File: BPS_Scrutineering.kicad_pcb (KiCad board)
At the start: 2 copper layers, 75 x 75 mm, 54 parts, among them SW1 SW_DIP_x07, SW2 SW_DIP_x07

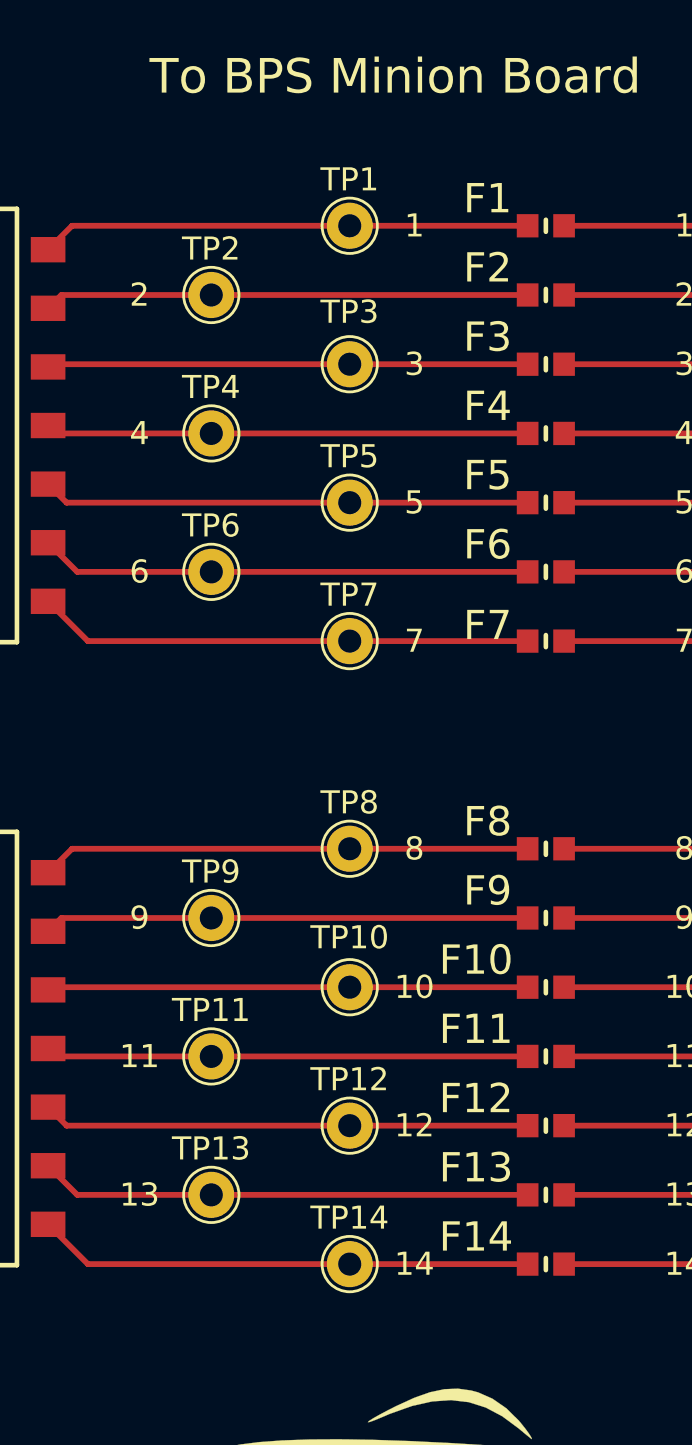
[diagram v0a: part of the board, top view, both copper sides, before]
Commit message: Changed testpoint footprints to match commonly-used testpoints
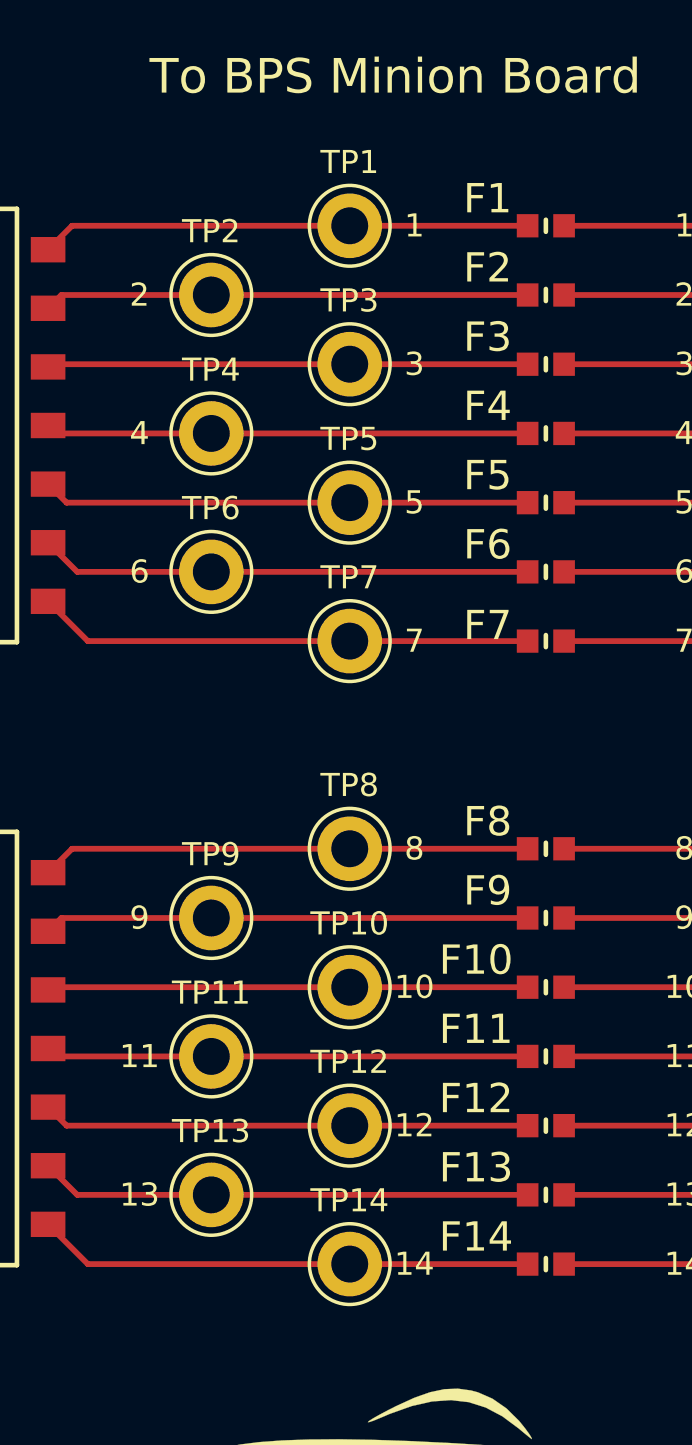
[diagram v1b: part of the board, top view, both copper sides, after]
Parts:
- TP1, TP10, TP11, TP12, TP13, TP14, TP2, TP3, TP4, TP5, TP6, TP7, TP8, TP9: footprint TestPoint:TestPoint_THTPad_D2.0mm_Drill1.0mm -> TestPoint:TestPoint_Keystone_5005-5009_Compact

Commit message: Finished Schematic
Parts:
- removed Dr_Hallock1: Dr. Hallock, UTSVT_Special:Hallock_Image
- removed H1, H2, H3, H4: MountingHole, MountingHole:MountingHole_3mm_Pad
- removed JC1, JC2, JC3, JC4: Conn_01x07, UTSVT_Connectors:Molex_Microfit+_01x07_Horizontal
- removed UTSVT_Logo1: UTSVT, UTSVT_Special:UTSVT_Logo_Symbol
- added F29: PTC Fuse, footprints:FUSC1810X100N, F.Cu at (171.2, 137.8)
- added F30: PTC Fuse, footprints:FUSC1810X100N, F.Cu at (171.2, 140.4)
- added F31: PTC Fuse, footprints:FUSC1810X100N, F.Cu at (171.2, 143.1)
- added F32: PTC Fuse, footprints:FUSC1810X100N, F.Cu at (171.2, 145.7)
- added F33: PTC Fuse, footprints:FUSC1810X100N, F.Cu at (171.2, 148.4)
- added F34: PTC Fuse, footprints:FUSC1810X100N, F.Cu at (171.2, 151.1)
- added F35: PTC Fuse, footprints:FUSC1810X100N, F.Cu at (171.2, 153.7)
- added F36: PTC Fuse, footprints:FUSC1810X100N, F.Cu at (171.2, 156.4)
- added F37: PTC Fuse, footprints:FUSC1810X100N, F.Cu at (100.6, 18.8)
- added F38: PTC Fuse, footprints:FUSC1810X100N, F.Cu at (100.6, 21.8)
- added F39: PTC Fuse, footprints:FUSC1810X100N, F.Cu at (100.6, 24.8)
- added F40: PTC Fuse, footprints:FUSC1810X100N, F.Cu at (100.6, 27.8)
- added F41: PTC Fuse, footprints:FUSC1810X100N, F.Cu at (100.6, 30.8)
- added F42: PTC Fuse, footprints:FUSC1810X100N, F.Cu at (100.6, 33.8)
- added F43: PTC Fuse, footprints:FUSC1810X100N, F.Cu at (100.6, 36.8)
- added F44: PTC Fuse, footprints:FUSC1810X100N, F.Cu at (100.6, 45.6)
- added F45: PTC Fuse, footprints:FUSC1810X100N, F.Cu at (100.6, 48.6)
- added F46: PTC Fuse, footprints:FUSC1810X100N, F.Cu at (100.6, 51.6)
- added F47: PTC Fuse, footprints:FUSC1810X100N, F.Cu at (100.6, 54.6)
- added F48: PTC Fuse, footprints:FUSC1810X100N, F.Cu at (100.6, 57.6)
- added F49: PTC Fuse, footprints:FUSC1810X100N, F.Cu at (100.6, 60.6)
- added F50: PTC Fuse, footprints:FUSC1810X100N, F.Cu at (100.6, 63.6)
- added F51: PTC Fuse, footprints:FUSC1810X100N, F.Cu at (100.7, 72.7)
- added F52: PTC Fuse, footprints:FUSC1810X100N, F.Cu at (100.6, 75.8)
- added F53: PTC Fuse, footprints:FUSC1810X100N, F.Cu at (100.6, 78.8)
- added F54: PTC Fuse, footprints:FUSC1810X100N, F.Cu at (100.6, 81.8)
- added F55: PTC Fuse, footprints:FUSC1810X100N, F.Cu at (100.6, 84.6)
- added F56: PTC Fuse, footprints:FUSC1810X100N, F.Cu at (100.6, 87.6)
- added F57: PTC Fuse, footprints:FUSC1810X100N, F.Cu at (100.6, 90.6)
- added F58: PTC Fuse, footprints:FUSC1810X100N, F.Cu at (100.6, 99.6)
- added F59: PTC Fuse, footprints:FUSC1810X100N, F.Cu at (100.6, 102.8)
- added F60: PTC Fuse, footprints:FUSC1810X100N, F.Cu at (100.6, 105.8)
- added F61: PTC Fuse, footprints:FUSC1810X100N, F.Cu at (100.6, 108.8)
- added F62: PTC Fuse, footprints:FUSC1810X100N, F.Cu at (100.6, 111.8)
- added F63: PTC Fuse, footprints:FUSC1810X100N, F.Cu at (100.6, 114.8)
- added F64: PTC Fuse, footprints:FUSC1810X100N, F.Cu at (100.6, 117.8)
- added F65: PTC Fuse, footprints:FUSC1810X100N, F.Cu at (100.6, 127.0)
- added F66: PTC Fuse, footprints:FUSC1810X100N, F.Cu at (100.6, 130.0)
- added F67: PTC Fuse, footprints:FUSC1810X100N, F.Cu at (100.6, 133.0)
- added F68: PTC Fuse, footprints:FUSC1810X100N, F.Cu at (100.6, 136.0)
- added F69: PTC Fuse, footprints:FUSC1810X100N, F.Cu at (100.6, 139.0)
- added F70: PTC Fuse, footprints:FUSC1810X100N, F.Cu at (100.6, 142.0)
- added F71: PTC Fuse, footprints:FUSC1810X100N, F.Cu at (100.6, 145.0)
- added F72: PTC Fuse, footprints:FUSC1810X100N, F.Cu at (100.6, 154.2)
- added F73: PTC Fuse, footprints:FUSC1810X100N, F.Cu at (100.6, 157.2)
- added F74: PTC Fuse, footprints:FUSC1810X100N, F.Cu at (100.6, 160.2)
- added F75: PTC Fuse, footprints:FUSC1810X100N, F.Cu at (100.6, 163.2)
- added F76: PTC Fuse, footprints:FUSC1810X100N, F.Cu at (100.6, 166.2)
- added F77: PTC Fuse, footprints:FUSC1810X100N, F.Cu at (100.8, 169.2)
- added F78: PTC Fuse, footprints:FUSC1810X100N, F.Cu at (100.8, 172.2)
- added J1: Conn_01x09, Connector_Molex:Molex_Micro-Fit_3.0_43650-0915_1x09_P3.00mm_Vertical, F.Cu at (246.4, 28.4)
- added J10: BottomConn, Connector_Molex:Molex_Micro-Fit_3.0_43650-0700_1x07_P3.00mm_Horizontal, F.Cu at (89.0, 172.2)
- added J2: Conn_01x09, Connector_Molex:Molex_Micro-Fit_3.0_43650-0915_1x09_P3.00mm_Vertical, F.Cu at (246.4, 61.8)
- added J3: Conn_01x09, Connector_Molex:Molex_Micro-Fit_3.0_43650-0915_1x09_P3.00mm_Vertical, F.Cu at (246.4, 94.8)
- added J4: Conn_01x09, Connector_Molex:Molex_Micro-Fit_3.0_43650-0915_1x09_P3.00mm_Vertical, F.Cu at (246.7, 128.2)
- added J5: TopConn, Connector_Molex:Molex_Micro-Fit_3.0_43650-0700_1x07_P3.00mm_Horizontal, F.Cu at (89.0, 36.8)
- added J6: BottomConn, Connector_Molex:Molex_Micro-Fit_3.0_43650-0700_1x07_P3.00mm_Horizontal, F.Cu at (88.8, 63.6)
- added J7: TopConn, Connector_Molex:Molex_Micro-Fit_3.0_43650-0700_1x07_P3.00mm_Horizontal, F.Cu at (89.0, 90.7)
- added J8: BottomConn, Connector_Molex:Molex_Micro-Fit_3.0_43650-0700_1x07_P3.00mm_Horizontal, F.Cu at (89.0, 117.8)
- added J9: TopConn, Connector_Molex:Molex_Micro-Fit_3.0_43650-0700_1x07_P3.00mm_Horizontal, F.Cu at (89.0, 145.0)
- added SW3: SW_DIP_x07, UTSVT_Special:7switch_module_DS04254207BKSMT, F.Cu at (147.0, 79.2)
- added SW4: SW_DIP_x07, UTSVT_Special:7switch_module_DS04254207BKSMT, F.Cu at (147.0, 107.8)
- added SW5: SW_DIP_x07, UTSVT_Special:7switch_module_DS04254207BKSMT, F.Cu at (147.2, 133.7)
- added SW6: SW_DIP_x07, UTSVT_Special:7switch_module_DS04254207BKSMT, F.Cu at (147.4, 159.8)
- added TP15: TestPoint, TestPoint:TestPoint_Keystone_5005-5009_Compact, F.Cu at (186.9, 63.6)
- added TP16: TestPoint, TestPoint:TestPoint_Keystone_5005-5009_Compact, F.Cu at (191.9, 53.5)
- added TP17: TestPoint, TestPoint:TestPoint_Keystone_5005-5009_Compact, F.Cu at (191.9, 58.6)
- added TP18: TestPoint, TestPoint:TestPoint_Keystone_5005-5009_Compact, F.Cu at (191.9, 63.6)
- added TP19: TestPoint, TestPoint:TestPoint_Keystone_5005-5009_Compact, F.Cu at (175.2, 98.7)
- added TP20: TestPoint, TestPoint:TestPoint_Keystone_5005-5009_Compact, F.Cu at (175.2, 103.8)
- added TP21: TestPoint, TestPoint:TestPoint_Keystone_5005-5009_Compact, F.Cu at (175.2, 108.8)
- added TP22: TestPoint, TestPoint:TestPoint_Keystone_5005-5009_Compact, F.Cu at (180.2, 98.7)
- added TP23: TestPoint, TestPoint:TestPoint_Keystone_5005-5009_Compact, F.Cu at (180.2, 103.8)
- added TP24: TestPoint, TestPoint:TestPoint_Keystone_5005-5009_Compact, F.Cu at (180.2, 108.8)
- added TP25: TestPoint, TestPoint:TestPoint_Keystone_5005-5009_Compact, F.Cu at (185.3, 98.7)
- added TP26: TestPoint, TestPoint:TestPoint_Keystone_5005-5009_Compact, F.Cu at (185.3, 103.8)
- added TP27: TestPoint, TestPoint:TestPoint_Keystone_5005-5009_Compact, F.Cu at (185.3, 108.8)
- added TP28: TestPoint, TestPoint:TestPoint_Keystone_5005-5009_Compact, F.Cu at (176.2, 132.3)
- added TP29: TestPoint, TestPoint:TestPoint_Keystone_5005-5009_Compact, F.Cu at (175.8, 141.3)
- added TP30: TestPoint, TestPoint:TestPoint_Keystone_5005-5009_Compact, F.Cu at (175.8, 146.4)
- added TP31: TestPoint, TestPoint:TestPoint_Keystone_5005-5009_Compact, F.Cu at (184.8, 132.9)
- added TP32: TestPoint, TestPoint:TestPoint_Keystone_5005-5009_Compact, F.Cu at (184.8, 137.9)
- added TP33: TestPoint, TestPoint:TestPoint_Keystone_5005-5009_Compact, F.Cu at (184.8, 143.0)
- added TP34: TestPoint, TestPoint:TestPoint_Keystone_5005-5009_Compact, F.Cu at (189.9, 132.9)
- added TP35: TestPoint, TestPoint:TestPoint_Keystone_5005-5009_Compact, F.Cu at (189.9, 137.9)
- added TP36: TestPoint, TestPoint:TestPoint_Keystone_5005-5009_Compact, F.Cu at (189.9, 143.0)
- added TP37: TestPoint, TestPoint:TestPoint_Keystone_5005-5009_Compact, F.Cu at (120.2, 19.7)
- added TP38: TestPoint, TestPoint:TestPoint_Keystone_5005-5009_Compact, F.Cu at (120.2, 24.8)
- added TP39: TestPoint, TestPoint:TestPoint_Keystone_5005-5009_Compact, F.Cu at (120.2, 29.8)
- added TP40: TestPoint, TestPoint:TestPoint_Keystone_5005-5009_Compact, F.Cu at (120.2, 34.9)
- added TP41: TestPoint, TestPoint:TestPoint_Keystone_5005-5009_Compact, F.Cu at (125.2, 19.7)
- added TP42: TestPoint, TestPoint:TestPoint_Keystone_5005-5009_Compact, F.Cu at (125.2, 24.8)
- added TP43: TestPoint, TestPoint:TestPoint_Keystone_5005-5009_Compact, F.Cu at (125.2, 29.8)
- added TP44: TestPoint, TestPoint:TestPoint_Keystone_5005-5009_Compact, F.Cu at (117.4, 45.9)
- added TP45: TestPoint, TestPoint:TestPoint_Keystone_5005-5009_Compact, F.Cu at (117.4, 51.0)
- added TP46: TestPoint, TestPoint:TestPoint_Keystone_5005-5009_Compact, F.Cu at (117.4, 56.0)
- added TP47: TestPoint, TestPoint:TestPoint_Keystone_5005-5009_Compact, F.Cu at (117.4, 61.1)
- added TP48: TestPoint, TestPoint:TestPoint_Keystone_5005-5009_Compact, F.Cu at (122.5, 45.9)
- added TP49: TestPoint, TestPoint:TestPoint_Keystone_5005-5009_Compact, F.Cu at (122.5, 51.0)
- added TP50: TestPoint, TestPoint:TestPoint_Keystone_5005-5009_Compact, F.Cu at (122.5, 56.0)
- added TP51: TestPoint, TestPoint:TestPoint_Keystone_5005-5009_Compact, F.Cu at (118.0, 73.3)
- added TP52: TestPoint, TestPoint:TestPoint_Keystone_5005-5009_Compact, F.Cu at (118.0, 78.3)
- added TP53: TestPoint, TestPoint:TestPoint_Keystone_5005-5009_Compact, F.Cu at (118.0, 83.4)
- added TP54: TestPoint, TestPoint:TestPoint_Keystone_5005-5009_Compact, F.Cu at (118.0, 88.4)
- added TP55: TestPoint, TestPoint:TestPoint_Keystone_5005-5009_Compact, F.Cu at (123.0, 73.3)
- added TP56: TestPoint, TestPoint:TestPoint_Keystone_5005-5009_Compact, F.Cu at (123.0, 78.3)
- added TP57: TestPoint, TestPoint:TestPoint_Keystone_5005-5009_Compact, F.Cu at (123.0, 83.4)
- added TP58: TestPoint, TestPoint:TestPoint_Keystone_5005-5009_Compact, F.Cu at (120.4, 101.1)
- added TP59: TestPoint, TestPoint:TestPoint_Keystone_5005-5009_Compact, F.Cu at (120.4, 106.2)
- added TP60: TestPoint, TestPoint:TestPoint_Keystone_5005-5009_Compact, F.Cu at (120.4, 111.2)
- added TP61: TestPoint, TestPoint:TestPoint_Keystone_5005-5009_Compact, F.Cu at (120.4, 116.3)
- added TP62: TestPoint, TestPoint:TestPoint_Keystone_5005-5009_Compact, F.Cu at (125.5, 101.1)
- added TP63: TestPoint, TestPoint:TestPoint_Keystone_5005-5009_Compact, F.Cu at (125.5, 106.2)
- added TP64: TestPoint, TestPoint:TestPoint_Keystone_5005-5009_Compact, F.Cu at (125.5, 111.2)
- added TP65: TestPoint, TestPoint:TestPoint_Keystone_5005-5009_Compact, F.Cu at (121.0, 128.5)
- added TP66: TestPoint, TestPoint:TestPoint_Keystone_5005-5009_Compact, F.Cu at (121.0, 133.5)
- added TP67: TestPoint, TestPoint:TestPoint_Keystone_5005-5009_Compact, F.Cu at (121.0, 138.6)
- added TP68: TestPoint, TestPoint:TestPoint_Keystone_5005-5009_Compact, F.Cu at (121.0, 143.6)
- added TP69: TestPoint, TestPoint:TestPoint_Keystone_5005-5009_Compact, F.Cu at (126.1, 128.5)
- added TP70: TestPoint, TestPoint:TestPoint_Keystone_5005-5009_Compact, F.Cu at (126.1, 133.5)
- added TP71: TestPoint, TestPoint:TestPoint_Keystone_5005-5009_Compact, F.Cu at (126.1, 138.6)
- added TP72: TestPoint, TestPoint:TestPoint_Keystone_5005-5009_Compact, F.Cu at (122.0, 155.2)
- added TP73: TestPoint, TestPoint:TestPoint_Keystone_5005-5009_Compact, F.Cu at (122.0, 160.2)
- added TP74: TestPoint, TestPoint:TestPoint_Keystone_5005-5009_Compact, F.Cu at (122.0, 165.3)
- added TP75: TestPoint, TestPoint:TestPoint_Keystone_5005-5009_Compact, F.Cu at (122.0, 170.3)
- added TP76: TestPoint, TestPoint:TestPoint_Keystone_5005-5009_Compact, F.Cu at (127.1, 155.2)
- added TP77: TestPoint, TestPoint:TestPoint_Keystone_5005-5009_Compact, F.Cu at (127.1, 160.2)
- added TP78: TestPoint, TestPoint:TestPoint_Keystone_5005-5009_Compact, F.Cu at (127.1, 165.3)
- F1, F15, F22, F8: footprint UTSVT_Special:ptc_fuse_FUSC1607X75N -> footprints:FUSC1810X100N
- F10, F11, F12, F13, F14, F16, F17, F18, F19, F2, F20, F21, F23, F24, F25, F26, F27, F28, F3, F4, F5, F6, F7, F9: value PTC_Fuse -> PTC Fuse; footprint UTSVT_Special:ptc_fuse_FUSC1607X75N -> footprints:FUSC1810X100N
- moved TP9 107.3 mm to (188.4, 30.7)
- moved TP8 105.3 mm to (188.4, 25.6)
- moved TP7 102.1 mm to (188.4, 20.6)
- moved TP13 98.0 mm to (186.9, 53.5)
- moved TP4 95.6 mm to (183.4, 20.6)
- moved TP6 92.6 mm to (183.4, 30.7)
- moved TP14 92.5 mm to (186.9, 58.6)
- moved TP5 90.3 mm to (183.4, 25.6)
- moved TP11 86.5 mm to (181.8, 58.6)
- moved TP2 84.0 mm to (178.3, 25.6)
- moved TP10 83.9 mm to (181.8, 53.5)
- moved F9 82.9 mm to (173.7, 40.7)
- moved F8 82.6 mm to (173.7, 38.0)
- moved F18 82.5 mm to (177.2, 73.6)
- moved F17 82.5 mm to (177.2, 71.0)
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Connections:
- F1 pad 1: Net-(F1-Pad1) -> /1-_BATT
- F1 pad 2: Net-(F1-Pad2) -> Net-(J1-Pin_1)
- F10 pad 1: Net-(F10-Pad1) -> /9-_BATT
- F10 pad 2: Net-(F10-Pad2) -> Net-(J2-Pin_1)
- F11 pad 1: Net-(F11-Pad1) -> /9+_BATT
- F11 pad 2: Net-(F11-Pad2) -> Net-(J2-Pin_2)
- F12 pad 1: Net-(F12-Pad1) -> /10+_BATT
- F12 pad 2: Net-(F12-Pad2) -> Net-(J2-Pin_3)
- F13 pad 1: Net-(F13-Pad1) -> /11+_BATT
- F13 pad 2: Net-(F13-Pad2) -> Net-(J2-Pin_4)
- F14 pad 1: Net-(F14-Pad1) -> /12+_BATT
- F14 pad 2: Net-(F14-Pad2) -> Net-(J2-Pin_5)
- F15 pad 1: Net-(F15-Pad1) -> /13+_BATT
- F15 pad 2: Net-(F15-Pad2) -> Net-(J2-Pin_6)
- F16 pad 1: Net-(F16-Pad1) -> /14+_BATT
- F16 pad 2: Net-(F16-Pad2) -> Net-(J2-Pin_7)
- F17 pad 1: Net-(F17-Pad1) -> /15+_BATT
- F17 pad 2: Net-(F17-Pad2) -> Net-(J2-Pin_8)
- F18 pad 1: Net-(F18-Pad1) -> /16+_BATT
- F18 pad 2: Net-(F18-Pad2) -> Net-(J2-Pin_9)
- F19 pad 1: Net-(F19-Pad1) -> /17-_BATT
- F19 pad 2: Net-(F19-Pad2) -> Net-(J3-Pin_1)
- F2 pad 1: Net-(F2-Pad1) -> /1+_BATT
- F2 pad 2: Net-(F2-Pad2) -> Net-(J1-Pin_2)
- F20 pad 1: Net-(F20-Pad1) -> /17+_BATT
- F20 pad 2: Net-(F20-Pad2) -> Net-(J3-Pin_2)
- F21 pad 1: Net-(F21-Pad1) -> /18+_BATT
- F21 pad 2: Net-(F21-Pad2) -> Net-(J3-Pin_3)
- F22 pad 1: Net-(F22-Pad1) -> /19+_BATT
- F22 pad 2: Net-(F22-Pad2) -> Net-(J3-Pin_4)
- F23 pad 1: Net-(F23-Pad1) -> /20+_BATT
- F23 pad 2: Net-(F23-Pad2) -> Net-(J3-Pin_5)
- F24 pad 1: Net-(F24-Pad1) -> /21+_BATT
- F24 pad 2: Net-(F24-Pad2) -> Net-(J3-Pin_6)
- F25 pad 1: Net-(F25-Pad1) -> /22+_BATT
- F25 pad 2: Net-(F25-Pad2) -> Net-(J3-Pin_7)
- F26 pad 1: Net-(F26-Pad1) -> /23+_BATT
- F26 pad 2: Net-(F26-Pad2) -> Net-(J3-Pin_8)
- F27 pad 1: Net-(F27-Pad1) -> /24+_BATT
- F27 pad 2: Net-(F27-Pad2) -> Net-(J3-Pin_9)
- F28 pad 1: Net-(F28-Pad1) -> /25-_BATT
- F28 pad 2: Net-(F28-Pad2) -> Net-(J4-Pin_1)
- F3 pad 1: Net-(F3-Pad1) -> /2+_BATT
- F3 pad 2: Net-(F3-Pad2) -> Net-(J1-Pin_3)
- F4 pad 1: Net-(F4-Pad1) -> /3+_BATT
- F4 pad 2: Net-(F4-Pad2) -> Net-(J1-Pin_4)
- F5 pad 1: Net-(F5-Pad1) -> /4+_BATT
- F5 pad 2: Net-(F5-Pad2) -> Net-(J1-Pin_5)
- F6 pad 1: Net-(F6-Pad1) -> /5+_BATT
- F6 pad 2: Net-(F6-Pad2) -> Net-(J1-Pin_6)
- F7 pad 1: Net-(F7-Pad1) -> /6+_BATT
- F7 pad 2: Net-(F7-Pad2) -> Net-(J1-Pin_7)
- F8 pad 1: Net-(F8-Pad1) -> /7+_BATT
- F8 pad 2: Net-(F8-Pad2) -> Net-(J1-Pin_8)
- F9 pad 1: Net-(F9-Pad1) -> /8+_BATT
- F9 pad 2: Net-(F9-Pad2) -> Net-(J1-Pin_9)
- SW1 pad 1: Net-(F1-Pad1) -> /BPS_MINION_1/Minion_Out_1
- SW1 pad 10: Net-(F19-Pad2) -> /4+_BATT
- SW1 pad 11: Net-(F6-Pad1) -> /BPS_MINION_1/Minion_Out_6
- SW1 pad 12: Net-(F20-Pad2) -> /5+_BATT
- SW1 pad 13: Net-(F7-Pad1) -> /BPS_MINION_1/Minion_Out_7
- SW1 pad 14: Net-(F21-Pad2) -> /6+_BATT
- SW1 pad 2: Net-(F15-Pad2) -> /1-_BATT
- SW1 pad 3: Net-(F2-Pad1) -> /BPS_MINION_1/Minion_Out_2
- SW1 pad 4: Net-(F16-Pad2) -> /1+_BATT
- SW1 pad 5: Net-(F3-Pad1) -> /BPS_MINION_1/Minion_Out_3
- SW1 pad 6: Net-(F17-Pad2) -> /2+_BATT
- SW1 pad 7: Net-(F4-Pad1) -> /BPS_MINION_1/Minion_Out_4
- SW1 pad 8: Net-(F18-Pad2) -> /3+_BATT
- SW1 pad 9: Net-(F5-Pad1) -> /BPS_MINION_1/Minion_Out_5
- SW2 pad 1: Net-(F8-Pad1) -> /BPS_MINION_1/Minion_Out_8
- SW2 pad 10: Net-(F26-Pad2) -> /11+_BATT
- SW2 pad 11: Net-(F13-Pad1) -> /BPS_MINION_1/Minion_Out_13
- SW2 pad 12: Net-(F27-Pad2) -> /DIP_SW_2/In_6
- SW2 pad 13: Net-(F14-Pad1) -> /BPS_MINION_1/Minion_Out_14
- SW2 pad 14: Net-(F28-Pad2) -> /DIP_SW_2/In_7
- SW2 pad 2: Net-(F22-Pad2) -> /7+_BATT
- SW2 pad 3: Net-(F9-Pad1) -> /BPS_MINION_1/Minion_Out_9
- SW2 pad 4: Net-(F23-Pad2) -> /8+_BATT
- SW2 pad 5: Net-(F10-Pad1) -> /BPS_MINION_1/Minion_Out_10
- SW2 pad 6: Net-(F24-Pad2) -> /9+_BATT
- SW2 pad 7: Net-(F11-Pad1) -> /BPS_MINION_1/Minion_Out_11
- SW2 pad 8: Net-(F25-Pad2) -> /10+_BATT
- SW2 pad 9: Net-(F12-Pad1) -> /BPS_MINION_1/Minion_Out_12
- TP1 pad 1: Net-(F1-Pad1) -> Net-(J1-Pin_1)
- TP10 pad 1: Net-(F10-Pad1) -> Net-(J2-Pin_1)
- TP11 pad 1: Net-(F11-Pad1) -> Net-(J2-Pin_2)
- TP12 pad 1: Net-(F12-Pad1) -> Net-(J2-Pin_3)
- TP13 pad 1: Net-(F13-Pad1) -> Net-(J2-Pin_4)
- TP14 pad 1: Net-(F14-Pad1) -> Net-(J2-Pin_5)
- TP2 pad 1: Net-(F2-Pad1) -> Net-(J1-Pin_2)
- TP3 pad 1: Net-(F3-Pad1) -> Net-(J1-Pin_3)
- TP4 pad 1: Net-(F4-Pad1) -> Net-(J1-Pin_4)
- TP5 pad 1: Net-(F5-Pad1) -> Net-(J1-Pin_5)
- TP6 pad 1: Net-(F6-Pad1) -> Net-(J1-Pin_6)
- TP7 pad 1: Net-(F7-Pad1) -> Net-(J1-Pin_7)
- TP8 pad 1: Net-(F8-Pad1) -> Net-(J1-Pin_8)
- TP9 pad 1: Net-(F9-Pad1) -> Net-(J1-Pin_9)
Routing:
- net Net-(F7-Pad1): track 21.5 -> 0.00 mm
- net Net-(F14-Pad1): track 21.5 -> 0.00 mm
- net Net-(F6-Pad1): track 21.3 -> 0.00 mm
- net Net-(F13-Pad1): track 21.3 -> 0.00 mm
- net Net-(F8-Pad1): track 21.2 -> 0.00 mm
- net Net-(F1-Pad1): track 21.2 -> 0.00 mm
- net Net-(F5-Pad1): track 21.1 -> 0.00 mm
- net Net-(F12-Pad1): track 21.1 -> 0.00 mm
- net Net-(F9-Pad1): track 21.0 -> 0.00 mm
- net Net-(F2-Pad1): track 21.0 -> 0.00 mm
- net Net-(F4-Pad1): track 20.9 -> 0.00 mm
- net Net-(F11-Pad1): track 20.9 -> 0.00 mm
- net Net-(F3-Pad1): track 20.8 -> 0.00 mm
- net Net-(F10-Pad1): track 20.8 -> 0.00 mm
- net Net-(F24-Pad1): track 9.22 -> 0.00 mm
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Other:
- board outline removed
- board text removed: "1"
- board text removed: "10"
- board text removed: "11"
- board text removed: "12"
- board text removed: "13"
- board text removed: "14"
- board text removed: "2"
- board text removed: "3"
- board text removed: "4"
- board text removed: "5"
- board text removed: "6"
- board text removed: "7"
- board text removed: "8"
- board text removed: "9"
- board text removed: "Dr. Gary Hallock"
- board text removed: "Jordan and Nandu were here"
- board text removed: "Pramuka was here"
- board text removed: "So was Chase"
- board text removed: "To BPS Minion Board"
- board text removed: "To Batteries"
- board text removed: "UTSVT - BPS Scrutineering v2.0 Fall 2022"

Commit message: twoWolves
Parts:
- removed F49, F50, F62, F63, F64, F77, F78: PTC Fuse, footprints:FUSC1810X100N
- removed TP49, TP50, TP62, TP63, TP64, TP77, TP78: TestPoint, TestPoint:TestPoint_Keystone_5005-5009_Compact
- moved J4 142.8 mm to (105.2, 147.6)
- moved J3 142.4 mm to (105.0, 111.1)
- moved J2 141.6 mm to (105.0, 66.6)
- moved J1 141.5 mm to (105.0, 30.6)
- moved TP17 110.2 mm to (86.5, 90.9)
- moved TP35 108.2 mm to (86.5, 169.9)
- moved TP7 106.1 mm to (86.0, 48.4)
- moved TP9 105.3 mm to (86.0, 55.4)
- moved TP16 104.5 mm to (93.0, 87.4)
- moved TP18 103.6 mm to (93.0, 94.4)
- moved TP25 103.5 mm to (86.5, 129.9)
- moved TP13 103.0 mm to (86.5, 76.9)
- moved TP27 102.7 mm to (86.5, 136.9)
- moved TP34 102.5 mm to (93.0, 166.4)
- moved TP15 102.4 mm to (86.5, 83.9)
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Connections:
- SW2 pad 11: /BPS_MINION_1/Minion_Out_13 -> /DIP_SW_2/Out_6
- SW2 pad 13: /BPS_MINION_1/Minion_Out_14 -> /DIP_SW_2/Out_7
- SW4 pad 11: /BPS_MINION_2/Minion_Out_13 -> /DIP_SW_4/Out_6
- SW4 pad 9: /BPS_MINION_2/Minion_Out_12 -> /DIP_SW_4/Out_5
- SW6 pad 11: /BPS_MINION_3/Minion_Out_13 -> /DIP_SW_6/Out_6
- SW6 pad 13: /BPS_MINION_3/Minion_Out_14 -> /DIP_SW_6/Out_7
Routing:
- net /BPS_MINION_3/Minion_Out_12: track 0.00 -> 29.3 mm
- net /BPS_MINION_3/Minion_Out_11: track 0.00 -> 28.7 mm
- net /BPS_MINION_3/Minion_Out_10: track 0.00 -> 28.1 mm
- net /BPS_MINION_2/Minion_Out_11: track 0.00 -> 28.1 mm
- net /BPS_MINION_3/Minion_Out_9: track 0.00 -> 27.5 mm
- net /BPS_MINION_2/Minion_Out_10: track 0.00 -> 27.5 mm
- net /BPS_MINION_1/Minion_Out_12: track 0.00 -> 27.2 mm
- net /BPS_MINION_3/Minion_Out_1: track 0.00 -> 27.1 mm
- net /BPS_MINION_3/Minion_Out_8: track 0.00 -> 26.9 mm
- net /BPS_MINION_2/Minion_Out_9: track 0.00 -> 26.8 mm
- net /BPS_MINION_1/Minion_Out_1: track 0.00 -> 26.7 mm
- net /BPS_MINION_1/Minion_Out_11: track 0.00 -> 26.5 mm
- net /BPS_MINION_2/Minion_Out_1: track 0.00 -> 26.5 mm
- net /BPS_MINION_3/Minion_Out_2: track 0.00 -> 26.5 mm
- net /BPS_MINION_2/Minion_Out_7: track 0.00 -> 26.4 mm
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- added copper zone on B.Cu, net (none)
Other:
- board outline added: 89 x 172 mm
